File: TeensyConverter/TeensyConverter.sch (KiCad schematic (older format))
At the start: 1 part

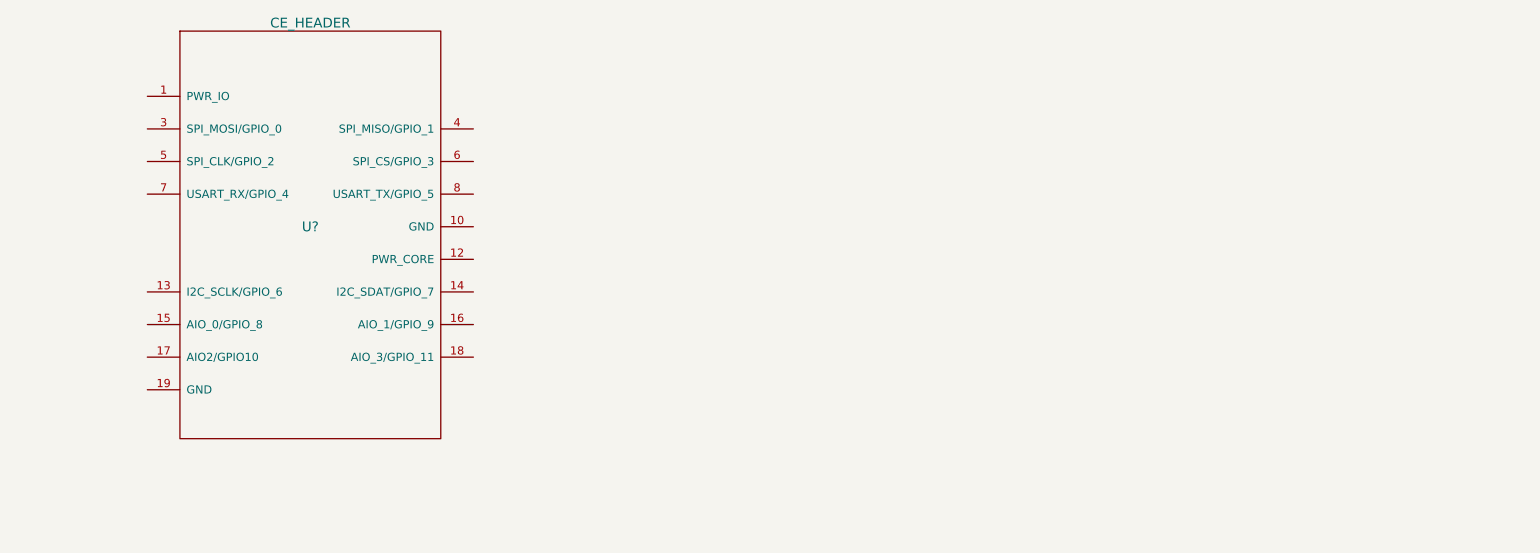
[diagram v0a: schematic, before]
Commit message: Added new directory for example project
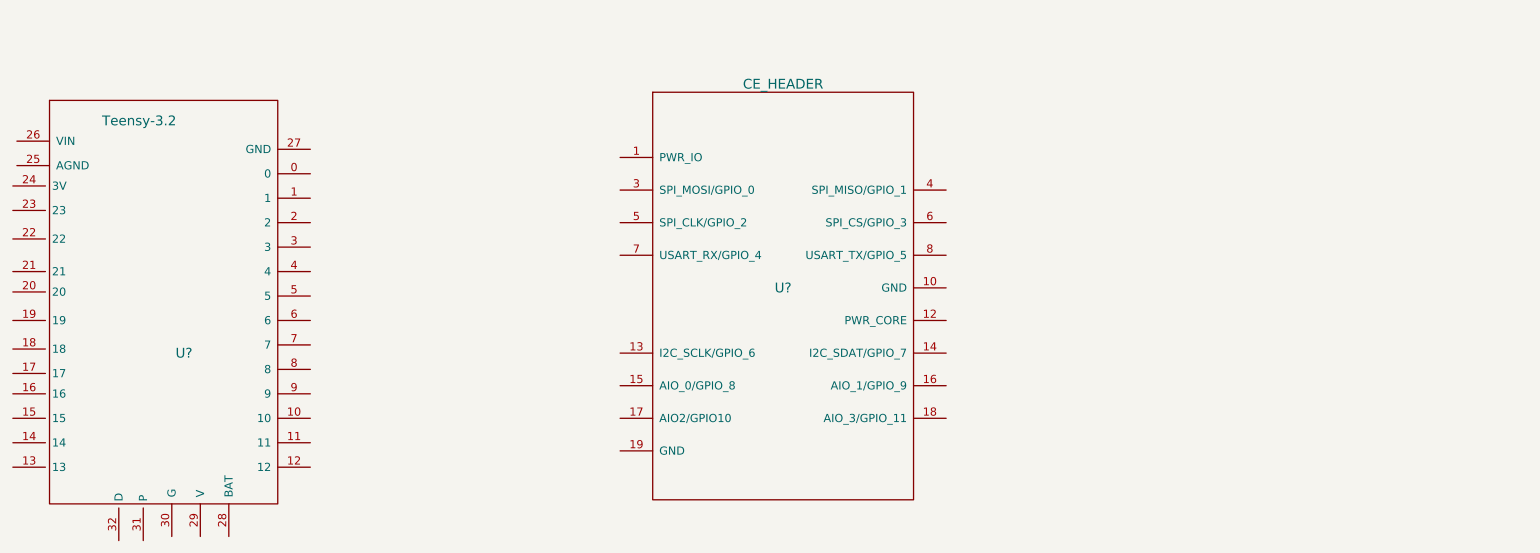
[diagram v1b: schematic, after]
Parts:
- removed U?: CE_HEADER, symbol CE_HEADER
- added U?: Teensy-3.2, symbol Teensy-3.2
- added U?: CE_HEADER, symbol CE_HEADER
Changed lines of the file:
@@
 EESchema Schematic File Version 2
-LIBS:CE Header-rescue
 LIBS:power
 LIBS:device
@@
 LIBS:contrib
 LIBS:valves
+LIBS:teensy-32
 LIBS:ce_header
-LIBS:CE Header-cache
 EELAYER 25 0
 EELAYER END
@@
 $EndDescr
 $Comp
-L CE_HEADER U?
-U 1 1 58A723CD
-P 3650 3250
-F 0 "U?" H 3650 3250 60  0000 C CNN
-F 1 "CE_HEADER" H 3650 4500 60  0000 C CNN
-F 2 "" H 3650 3250 60  0001 C CNN
-F 3 "" H 3650 3250 60  0001 C CNN
-	1    3650 3250
+L Teensy-3.2 U?
+U 1 1 58A73DD8
+P 2725 3775
+F 0 "U?" H 2875 3525 60  0000 C CNN
+F 1 "Teensy-3.2" H 2600 4950 60  0000 C CNN
+F 2 "" H 2500 3450 60  0001 C CNN
+F 3 "" H 2500 3450 60  0001 C CNN
+	1    2725 3775
 	1    0    0    -1
 $EndComp
+$Comp
+L CE_HEADER U?
+U 1 1 58A73E7D
+P 6550 3625
+F 0 "U?" H 6550 3625 60  0000 C CNN
+F 1 "CE_HEADER" H 6550 4875 60  0000 C CNN
+F 2 "" H 6550 3625 60  0001 C CNN
+F 3 "" H 6550 3625 60  0001 C CNN
+	1    6550 3625
+	1    0    0    -1
+$EndComp

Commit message: Connected teensy header to ce header
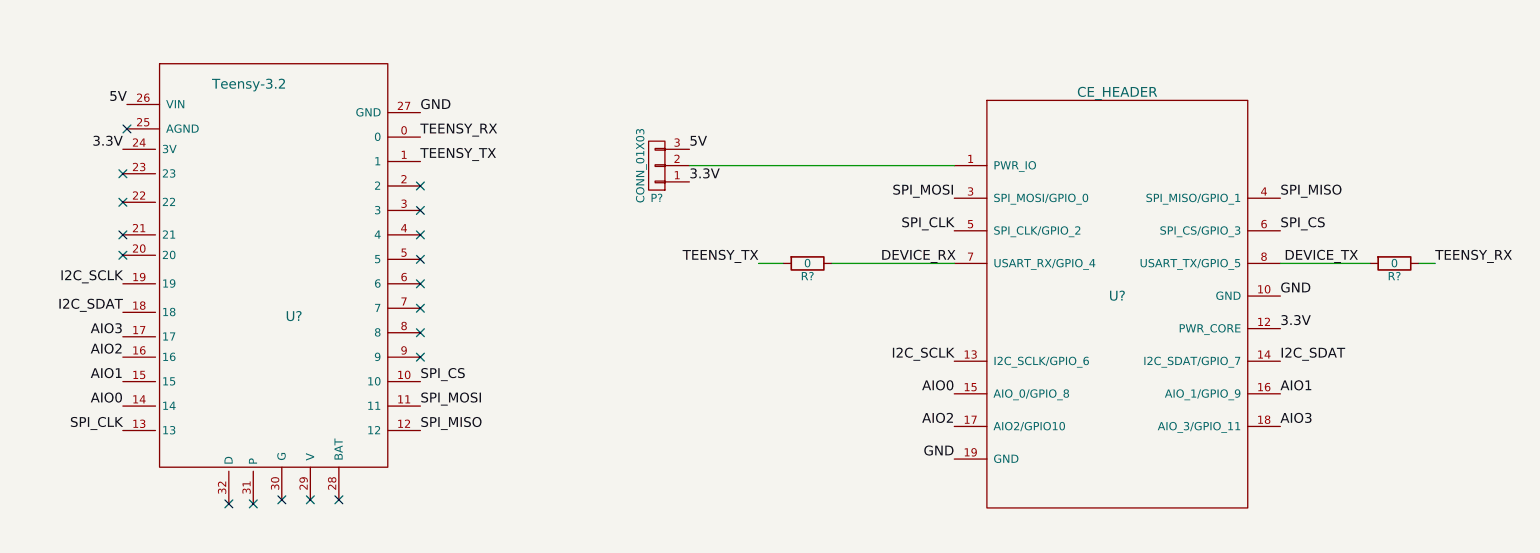
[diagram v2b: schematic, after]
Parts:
- added P?: CONN_01X03, symbol CONN_01X03
- added R? (x2): 0, symbol R
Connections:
- net TEENSY_RX: now reaches U?.0
- net TEENSY_RX: now also R?.1
- net TEENSY_TX: now reaches U?.1
- net TEENSY_TX: now also R?.2
- net SPI_CS: now reaches U?.10
- net SPI_CS: now also U?.6 (SPI_CS/GPIO_3)
- net SPI_MOSI: now reaches U?.11
- net SPI_MOSI: now also U?.3 (SPI_MOSI/GPIO_0)
- net SPI_MISO: now reaches U?.12
- net SPI_MISO: now also U?.4 (SPI_MISO/GPIO_1)
- net SPI_CLK: now reaches U?.13
- net SPI_CLK: now also U?.5 (SPI_CLK/GPIO_2)
- net AIO0: now reaches U?.14
- net AIO0: now also U?.15 (AIO_0/GPIO_8)
- net AIO1: now reaches U?.15
- net AIO1: now also U?.16 (AIO_1/GPIO_9)
- net AIO2: now reaches U?.16
- net AIO2: now also U?.17 (AIO2/GPIO10)
- net AIO3: now reaches U?.17
- net AIO3: now also U?.18 (AIO_3/GPIO_11)
- net I2C_SDAT: now reaches U?.18
- net I2C_SDAT: now also U?.14 (I2C_SDAT/GPIO_7)
- net I2C_SCLK: now reaches U?.19
- net I2C_SCLK: now also U?.13 (I2C_SCLK/GPIO_6)
- net 3.3V: now reaches U?.24 (3V)
- net 3.3V: now also U?.12 (PWR_CORE), P?.1 (P1)
- net 5V: now reaches U?.26 (VIN)
- net 5V: now also P?.3 (P3)
- net GND: now reaches U?.27 (GND)
- net GND: now also U?.10 (GND), U?.19 (GND)
- net at U?.1 (PWR_IO): now also P?.2 (P2)
- net DEVICE_RX: now reaches U?.7 (USART_RX/GPIO_4)
- net DEVICE_RX: now also R?.1
- net DEVICE_TX: now reaches U?.8 (USART_TX/GPIO_5)
- net DEVICE_TX: now also R?.2
- no-connect marks 0 -> 18
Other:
- moved on the sheet: U?
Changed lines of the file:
@@
 L Teensy-3.2 U?
 U 1 1 58A73DD8
-P 2725 3775
-F 0 "U?" H 2875 3525 60  0000 C CNN
-F 1 "Teensy-3.2" H 2600 4950 60  0000 C CNN
-F 2 "" H 2500 3450 60  0001 C CNN
-F 3 "" H 2500 3450 60  0001 C CNN
-	1    2725 3775
+P 3400 3550
+F 0 "U?" H 3550 3300 60  0000 C CNN
+F 1 "Teensy-3.2" H 3275 4725 60  0000 C CNN
+F 2 "" H 3175 3225 60  0001 C CNN
+F 3 "" H 3175 3225 60  0001 C CNN
+	1    3400 3550
 	1    0    0    -1
 $EndComp
@@
 L CE_HEADER U?
 U 1 1 58A73E7D
-P 6550 3625
-F 0 "U?" H 6550 3625 60  0000 C CNN
-F 1 "CE_HEADER" H 6550 4875 60  0000 C CNN
-F 2 "" H 6550 3625 60  0001 C CNN
-F 3 "" H 6550 3625 60  0001 C CNN
-	1    6550 3625
+P 8600 3675
+F 0 "U?" H 8600 3675 60  0000 C CNN
+F 1 "CE_HEADER" H 8600 4925 60  0000 C CNN
+F 2 "" H 8600 3675 60  0001 C CNN
+F 3 "" H 8600 3675 60  0001 C CNN
+	1    8600 3675
 	1    0    0    -1
 $EndComp
+Text Label 2500 2775 2    60   ~ 0
+3.3V
+Wire Wire Line
+	7600 2875 5975 2875
+$Comp
+L CONN_01X03 P?
+U 1 1 58A74996
+P 5775 2875
+F 0 "P?" H 5775 3075 50  0000 C CNN
+F 1 "CONN_01X03" V 5875 2875 50  0000 C CNN
+F 2 "" H 5775 2875 50  0000 C CNN
+F 3 "" H 5775 2875 50  0000 C CNN
+	1    5775 2875
+	-1   0    0    1
+$EndComp
+Text Label 9600 3875 0    60   ~ 0
+3.3V
+Text Label 5975 2975 0    60   ~ 0
+3.3V
+Text Label 2525 2500 2    60   ~ 0
+5V
+Text Label 5975 2775 0    60   ~ 0
+5V
+Text Label 9600 3675 0    60   ~ 0
+GND
+Text Label 4325 2550 0    60   ~ 0
+GND
+Text Label 7600 4675 2    60   ~ 0
+GND
+Text Label 7600 3075 2    60   ~ 0
+SPI_MOSI
+Text Label 4325 4350 0    60   ~ 0
+SPI_MOSI
+Text Label 7600 3275 2    60   ~ 0
+SPI_CLK
+Text Label 2500 4500 2    60   ~ 0
+SPI_CLK
+Text Label 9600 3075 0    60   ~ 0
+SPI_MISO
+Text Label 4325 4500 0    60   ~ 0
+SPI_MISO
+Text Label 9600 3275 0    60   ~ 0
+SPI_CS
+Text Label 4325 4200 0    60   ~ 0
+SPI_CS
+$Comp
+L R R?
+U 1 1 58A768E3
+P 6700 3475
+F 0 "R?" V 6780 3475 50  0000 C CNN
+F 1 "0" V 6700 3475 50  0000 C CNN
+F 2 "" V 6630 3475 50  0000 C CNN
+F 3 "" H 6700 3475 50  0000 C CNN
+	1    6700 3475
+	0    1    1    0
+$EndComp
+Wire Wire Line
+	7600 3475 6850 3475
+$Comp
+L R R?
+U 1 1 58A76B77
+P 10300 3475
+F 0 "R?" V 10380 3475 50  0000 C CNN
+F 1 "0" V 10300 3475 50  0000 C CNN
+F 2 "" V 10230 3475 50  0000 C CNN
+F 3 "" H 10300 3475 50  0000 C CNN
+	1    10300 3475
+	0    1    1    0
+$EndComp
+Wire Wire Line
+	10150 3475 9600 3475
+Wire Wire Line
+	6550 3475 6400 3475
+Wire Wire Line
+	10450 3475 10550 3475
+Text Label 9625 3475 0    60   ~ 0
+DEVICE_TX
+Text Label 10550 3475 0    60   ~ 0
+TEENSY_RX
+Text Label 4325 2700 0    60   ~ 0
+TEENSY_RX
+Text Label 7150 3475 0    60   ~ 0
+DEVICE_RX
+Text Label 6400 3475 2    60   ~ 0
+TEENSY_TX
+Text Label 4325 2850 0    60   ~ 0
+TEENSY_TX
+Text Label 7600 4075 2    60   ~ 0
+I2C_SCLK
+Text Label 2500 3600 2    60   ~ 0
+I2C_SCLK
+Text Label 9600 4075 0    60   ~ 0
+I2C_SDAT
+Text Label 2500 3775 2    60   ~ 0
+I2C_SDAT
+Text Label 7600 4275 2    60   ~ 0
+AIO0
+Text Label 2500 4350 2    60   ~ 0
+AIO0
+Text Label 2500 4200 2    60   ~ 0
+AIO1
+Text Label 2500 4050 2    60   ~ 0
+AIO2
+Text Label 2500 3925 2    60   ~ 0
+AIO3
+Text Label 7600 4475 2    60   ~ 0
+AIO2
+Text Label 9600 4275 0    60   ~ 0
+AIO1
+Text Label 9600 4475 0    60   ~ 0
+AIO3
+NoConn ~ 4325 3000
+NoConn ~ 4325 3150
+NoConn ~ 4325 3300
+NoConn ~ 4325 3450
+NoConn ~ 4325 3600
+NoConn ~ 4325 3750
+NoConn ~ 4325 3900
+NoConn ~ 4325 4050
+NoConn ~ 3825 4925
+NoConn ~ 3650 4925
+NoConn ~ 3475 4925
+NoConn ~ 3300 4950
+NoConn ~ 3150 4950
+NoConn ~ 2525 2650
+NoConn ~ 2500 2925
+NoConn ~ 2500 3100
+NoConn ~ 2500 3300
+NoConn ~ 2500 3425
 $EndSCHEMATC

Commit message: Associated components and added to layout
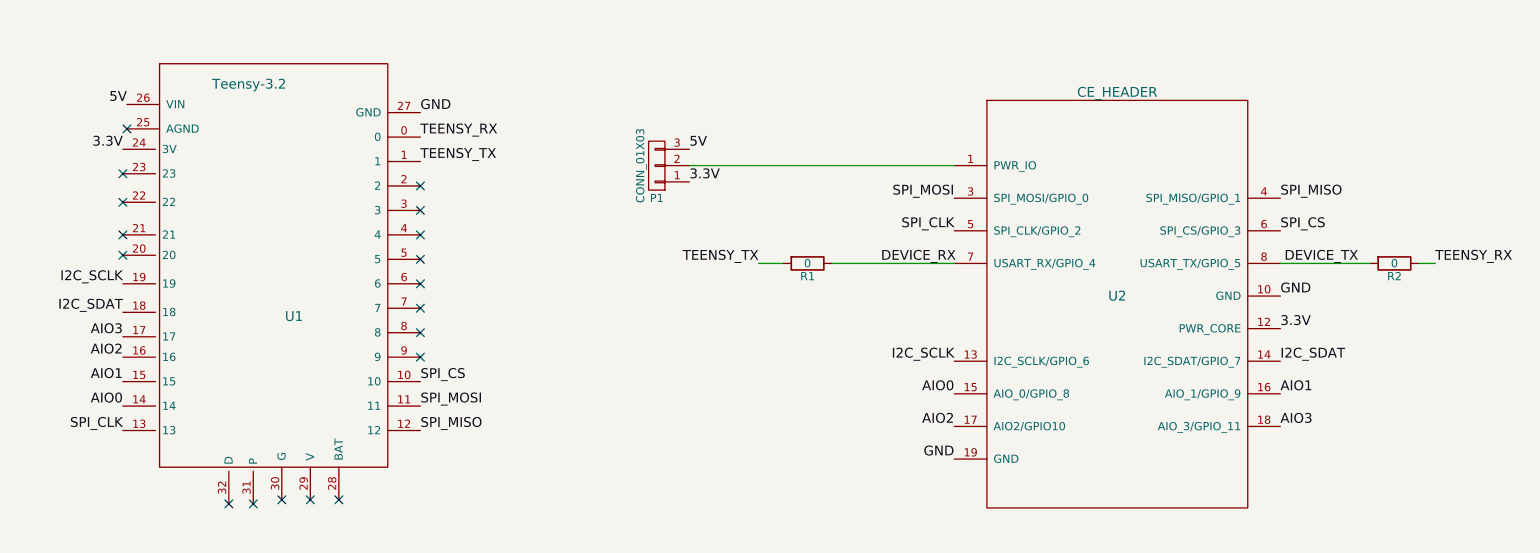
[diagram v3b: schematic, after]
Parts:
- P1: renamed from P?; footprint (none) -> Pin_Headers:Pin_Header_Straight_1x03_Pitch2.54mm
- R1, R2: renamed from R?; footprint (none) -> Resistors_SMD:R_0805_HandSoldering
- U1: renamed from U?; footprint (none) -> TeensyConverter:Teensy-32
- gave numbers to parts that had none: 1
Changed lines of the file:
@@
 LIBS:teensy-32
 LIBS:ce_header
+LIBS:TeensyConverter-cache
 EELAYER 25 0
 EELAYER END
@@
 $EndDescr
 $Comp
-L Teensy-3.2 U?
+L Teensy-3.2 U1
 U 1 1 58A73DD8
 P 3400 3550
-F 0 "U?" H 3550 3300 60  0000 C CNN
+F 0 "U1" H 3550 3300 60  0000 C CNN
 F 1 "Teensy-3.2" H 3275 4725 60  0000 C CNN
-F 2 "" H 3175 3225 60  0001 C CNN
+F 2 "TeensyConverter:Teensy-32" H 3175 3225 60  0001 C CNN
 F 3 "" H 3175 3225 60  0001 C CNN
 	1    3400 3550
@@
 $EndComp
 $Comp
-L CE_HEADER U?
+L CE_HEADER U2
 U 1 1 58A73E7D
 P 8600 3675
-F 0 "U?" H 8600 3675 60  0000 C CNN
+F 0 "U2" H 8600 3675 60  0000 C CNN
 F 1 "CE_HEADER" H 8600 4925 60  0000 C CNN
 F 2 "" H 8600 3675 60  0001 C CNN
@@
 	7600 2875 5975 2875
 $Comp
-L CONN_01X03 P?
+L CONN_01X03 P1
 U 1 1 58A74996
 P 5775 2875
-F 0 "P?" H 5775 3075 50  0000 C CNN
+F 0 "P1" H 5775 3075 50  0000 C CNN
 F 1 "CONN_01X03" V 5875 2875 50  0000 C CNN
-F 2 "" H 5775 2875 50  0000 C CNN
+F 2 "Pin_Headers:Pin_Header_Straight_1x03_Pitch2.54mm" H 5775 2875 50  0001 C CNN
 F 3 "" H 5775 2875 50  0000 C CNN
 	1    5775 2875
@@
 SPI_CS
 $Comp
-L R R?
+L R R1
 U 1 1 58A768E3
 P 6700 3475
-F 0 "R?" V 6780 3475 50  0000 C CNN
+F 0 "R1" V 6780 3475 50  0000 C CNN
 F 1 "0" V 6700 3475 50  0000 C CNN
-F 2 "" V 6630 3475 50  0000 C CNN
+F 2 "Resistors_SMD:R_0805_HandSoldering" V 6630 3475 50  0001 C CNN
 F 3 "" H 6700 3475 50  0000 C CNN
 	1    6700 3475
@@
 	7600 3475 6850 3475
 $Comp
-L R R?
+L R R2
 U 1 1 58A76B77
 P 10300 3475
-F 0 "R?" V 10380 3475 50  0000 C CNN
+F 0 "R2" V 10380 3475 50  0000 C CNN
 F 1 "0" V 10300 3475 50  0000 C CNN
-F 2 "" V 10230 3475 50  0000 C CNN
+F 2 "Resistors_SMD:R_0805_HandSoldering" V 10230 3475 50  0001 C CNN
 F 3 "" H 10300 3475 50  0000 C CNN
 	1    10300 3475

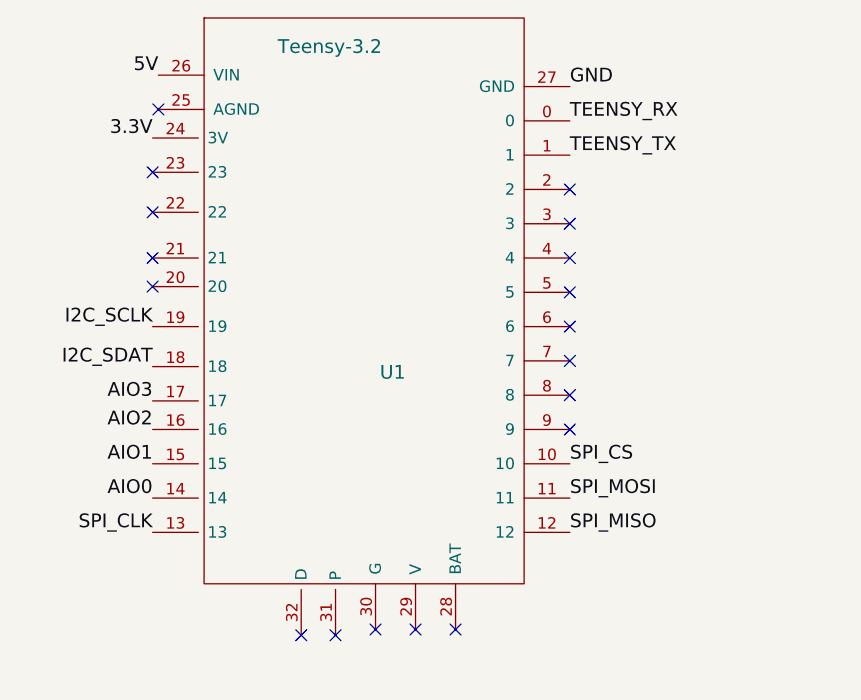
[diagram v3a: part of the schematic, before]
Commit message: Finished layout of CE header converter for Teensy with flipped footprints
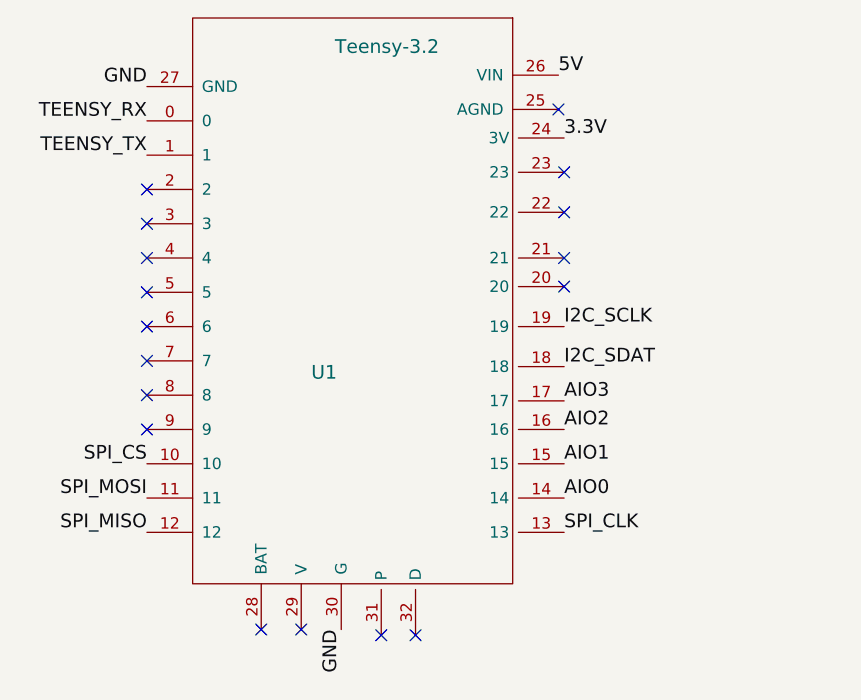
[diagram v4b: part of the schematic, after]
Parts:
- U2: footprint (none) -> TeensyConverter:CE_Header
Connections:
- net GND: now also U1.30 (G)
- no-connect marks 18 -> 17
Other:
- moved on the sheet: U1
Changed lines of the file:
@@
 F 3 "" H 3175 3225 60  0001 C CNN
 	1    3400 3550
-	1    0    0    -1
+	-1   0    0    -1
 $EndComp
 $Comp
@@
 F 0 "U2" H 8600 3675 60  0000 C CNN
 F 1 "CE_HEADER" H 8600 4925 60  0000 C CNN
-F 2 "" H 8600 3675 60  0001 C CNN
+F 2 "TeensyConverter:CE_Header" H 8600 3675 60  0001 C CNN
 F 3 "" H 8600 3675 60  0001 C CNN
 	1    8600 3675
 	1    0    0    -1
 $EndComp
-Text Label 2500 2775 2    60   ~ 0
+Text Label 4300 2775 0    60   ~ 0
 3.3V
 Wire Wire Line
@@
 Text Label 5975 2975 0    60   ~ 0
 3.3V
-Text Label 2525 2500 2    60   ~ 0
+Text Label 4275 2500 0    60   ~ 0
 5V
 Text Label 5975 2775 0    60   ~ 0
@@
 Text Label 9600 3675 0    60   ~ 0
 GND
-Text Label 4325 2550 0    60   ~ 0
+Text Label 2475 2550 2    60   ~ 0
 GND
 Text Label 7600 4675 2    60   ~ 0
@@
 Text Label 7600 3075 2    60   ~ 0
 SPI_MOSI
-Text Label 4325 4350 0    60   ~ 0
+Text Label 2475 4350 2    60   ~ 0
 SPI_MOSI
 Text Label 7600 3275 2    60   ~ 0
 SPI_CLK
-Text Label 2500 4500 2    60   ~ 0
+Text Label 4300 4500 0    60   ~ 0
 SPI_CLK
 Text Label 9600 3075 0    60   ~ 0
 SPI_MISO
-Text Label 4325 4500 0    60   ~ 0
+Text Label 2475 4500 2    60   ~ 0
 SPI_MISO
 Text Label 9600 3275 0    60   ~ 0
 SPI_CS
-Text Label 4325 4200 0    60   ~ 0
+Text Label 2475 4200 2    60   ~ 0
 SPI_CS
 $Comp
@@
 Text Label 10550 3475 0    60   ~ 0
 TEENSY_RX
-Text Label 4325 2700 0    60   ~ 0
+Text Label 2475 2700 2    60   ~ 0
 TEENSY_RX
 Text Label 7150 3475 0    60   ~ 0
@@
 Text Label 6400 3475 2    60   ~ 0
 TEENSY_TX
-Text Label 4325 2850 0    60   ~ 0
+Text Label 2475 2850 2    60   ~ 0
 TEENSY_TX
 Text Label 7600 4075 2    60   ~ 0
 I2C_SCLK
-Text Label 2500 3600 2    60   ~ 0
+Text Label 4300 3600 0    60   ~ 0
 I2C_SCLK
 Text Label 9600 4075 0    60   ~ 0
 I2C_SDAT
-Text Label 2500 3775 2    60   ~ 0
+Text Label 4300 3775 0    60   ~ 0
 I2C_SDAT
 Text Label 7600 4275 2    60   ~ 0
 AIO0
-Text Label 2500 4350 2    60   ~ 0
+Text Label 4300 4350 0    60   ~ 0
 AIO0
-Text Label 2500 4200 2    60   ~ 0
+Text Label 4300 4200 0    60   ~ 0
 AIO1
-Text Label 2500 4050 2    60   ~ 0
+Text Label 4300 4050 0    60   ~ 0
 AIO2
-Text Label 2500 3925 2    60   ~ 0
+Text Label 4300 3925 0    60   ~ 0
 AIO3
 Text Label 7600 4475 2    60   ~ 0
@@
 Text Label 9600 4475 0    60   ~ 0
 AIO3
-NoConn ~ 4325 3000
-NoConn ~ 4325 3150
-NoConn ~ 4325 3300
-NoConn ~ 4325 3450
-NoConn ~ 4325 3600
-NoConn ~ 4325 3750
-NoConn ~ 4325 3900
-NoConn ~ 4325 4050
-NoConn ~ 3825 4925
-NoConn ~ 3650 4925
-NoConn ~ 3475 4925
-NoConn ~ 3300 4950
-NoConn ~ 3150 4950
-NoConn ~ 2525 2650
-NoConn ~ 2500 2925
-NoConn ~ 2500 3100
-NoConn ~ 2500 3300
-NoConn ~ 2500 3425
+NoConn ~ 2475 3000
+NoConn ~ 2475 3150
+NoConn ~ 2475 3300
+NoConn ~ 2475 3450
+NoConn ~ 2475 3600
+NoConn ~ 2475 3750
+NoConn ~ 2475 3900
+NoConn ~ 2475 4050
+NoConn ~ 2975 4925
+NoConn ~ 3150 4925
+NoConn ~ 3500 4950
+NoConn ~ 3650 4950
+NoConn ~ 4275 2650
+NoConn ~ 4300 2925
+NoConn ~ 4300 3100
+NoConn ~ 4300 3300
+NoConn ~ 4300 3425
+Text Label 3325 4925 3    60   ~ 0
+GND
 $EndSCHEMATC
